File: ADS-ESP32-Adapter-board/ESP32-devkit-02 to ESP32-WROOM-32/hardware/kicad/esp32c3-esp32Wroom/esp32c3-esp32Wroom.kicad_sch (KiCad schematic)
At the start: 4 parts, among them J1 Conn_01x15_esp32_devkit_V1_el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, J2 Conn_01x15_esp32_devkit_V1_el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, J3 Conn_01x15_esp32_c3_devkit_02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, J4 Conn_01x15_esp32_c3_devkit_02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

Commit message: modified
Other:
- company: (none) -> BIOMEC UMA dpto Hardware
- title: (none) -> ESP32-C3-DevkitC-02
- moved on the sheet: J1, J2, J3, J4

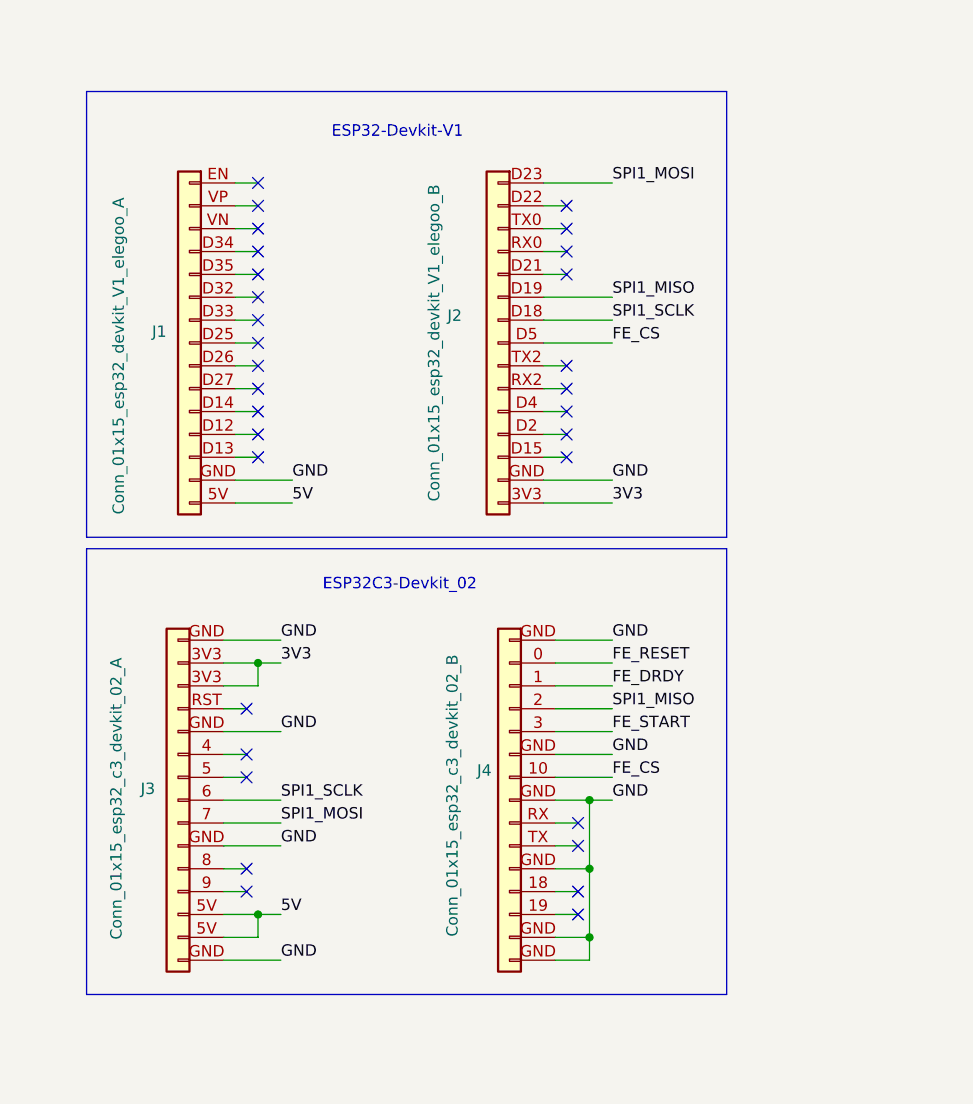
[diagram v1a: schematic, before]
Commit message: Esquema terminado, PCB terminada pero falta agregar algún símbolo que indique la posición, asegurar que las ancho pistas es adecuado y que no haya acoplamiento entre pistas.
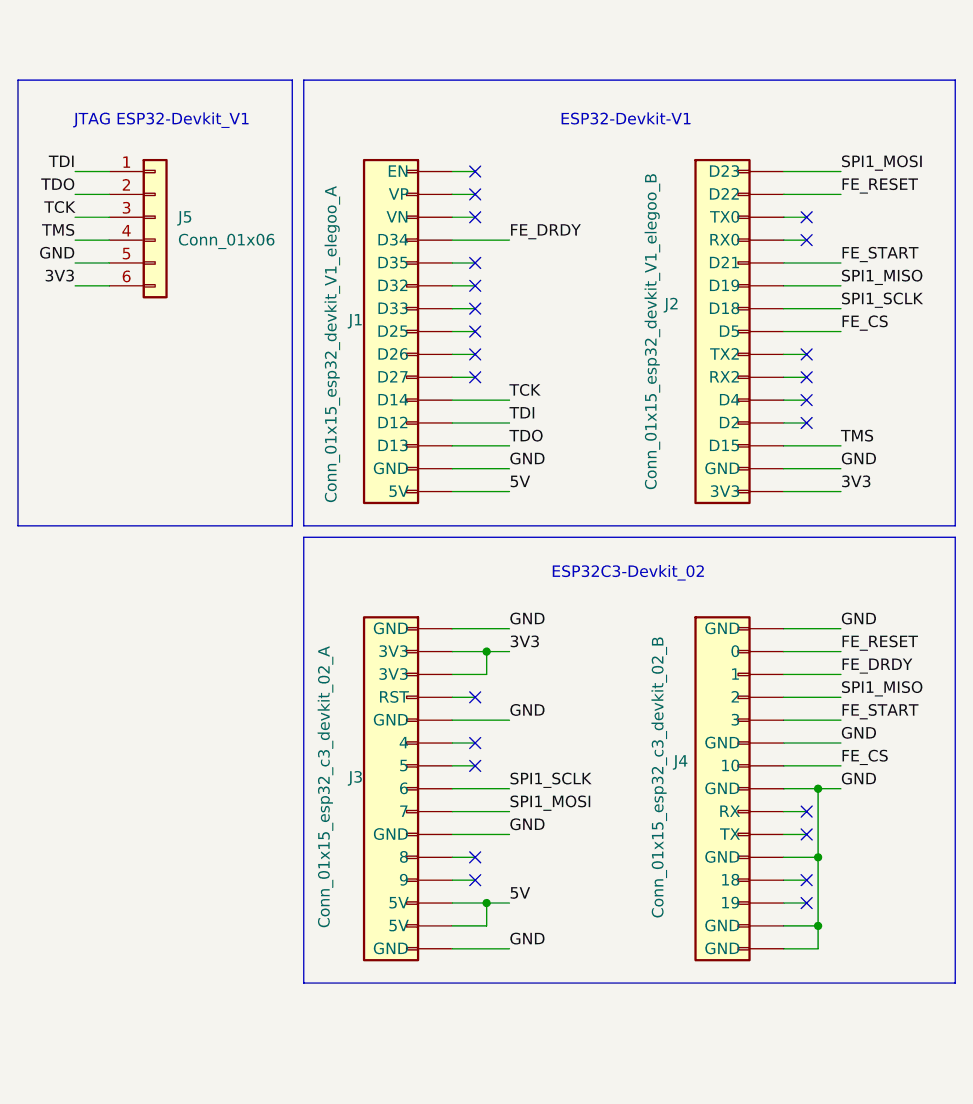
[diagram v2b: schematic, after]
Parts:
- added J5: Conn_01x06, Connector_PinSocket_2.54mm:PinSocket_1x06_P2.54mm_Vertical, symbol Connector_Generic:Conn_01x06
- J1, J2: footprint Connector_PinSocket_2.54mm:PinSocket_1x15_P2.54mm_Vertical -> Connector_PinHeader_2.54mm:PinHeader_1x15_P2.54mm_Vertical
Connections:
- net 3V3: now also J2.15 (3V3), J3.2 (3V3), J3.3 (3V3), J5.6 (Pin_6); no longer J2.3V3 (Pin_15), J3.3V3 (Pin_3)
- net 5V: now also J1.15 (5V), J3.13 (5V), J3.14 (5V); no longer J1.5V (Pin_15), J3.5V (Pin_14)
- net FE_CS: now also J2.8 (D5), J4.7 (10); no longer J2.D5 (Pin_8), J4.10 (Pin_7)
- net FE_DRDY: now also J1.4 (D34), J4.3 (1); no longer J4.1 (Pin_3)
- net FE_RESET: now also J2.2 (D22), J4.2 (0); no longer J4.0 (Pin_2)
- net FE_START: now also J2.5 (D21), J4.5 (3); no longer J4.3 (Pin_5)
- net GND: now also J1.14 (GND), J2.14 (GND), J3.1 (GND), J3.10 (GND), J3.15 (GND), J3.5 (GND), J4.1 (GND), J4.11 (GND), J4.14 (GND), J4.15 (GND), J4.6 (GND), J4.8 (GND), J5.5 (Pin_5); no longer J1.GND (Pin_14), J2.GND (Pin_14), J3.GND (Pin_15), J4.GND (Pin_15)
- net SPI1_MISO: now also J2.6 (D19), J4.4 (2); no longer J2.D19 (Pin_6), J4.2 (Pin_4)
- net SPI1_MOSI: now also J2.1 (D23), J3.9 (7); no longer J2.D23 (Pin_1), J3.7 (Pin_9)
- net SPI1_SCLK: now also J2.7 (D18), J3.8 (6); no longer J2.D18 (Pin_7), J3.6 (Pin_8)
- new net TCK: J1.11 (D14), J5.3 (Pin_3)
- new net TDI: J1.12 (D12), J5.1 (Pin_1)
- new net TDO: J1.13 (D13), J5.2 (Pin_2)
- new net TMS: J2.13 (D15), J5.4 (Pin_4)
- no-connect marks 31 -> 24
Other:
- note added: "JTAG ESP32-Devkit_V1"
- moved on the sheet: J1, J2, J3, J4

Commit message: Refactor code structure for improved readability and maintainability
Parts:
- J1, J2: footprint Connector_PinHeader_2.54mm:PinHeader_1x15_P2.54mm_Vertical -> Connector_PinSocket_2.54mm:PinSocket_1x15_P2.54mm_Vertical
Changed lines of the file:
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@@
 			)
 		)
-		(property "Footprint" "Connector_PinHeader_2.54mm:PinHeader_1x15_P2.54mm_Vertical"
+		(property "Footprint" "Connector_PinSocket_2.54mm:PinSocket_1x15_P2.54mm_Vertical"
 			(at 107.95 52.07 0)
 			(hide yes)
@@
 			)
 		)
-		(property "Footprint" "Connector_PinHeader_2.54mm:PinHeader_1x15_P2.54mm_Vertical"
+		(property "Footprint" "Connector_PinSocket_2.54mm:PinSocket_1x15_P2.54mm_Vertical"
 			(at 73.66 52.07 0)
 			(hide yes)

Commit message: Add additional text annotations to schematic and update visible layers in PCB layout
- Added JTAG, GND, GPIO, Source, and SPI text annotations to the schematic for better clarity and reference.
- Updated the visible layers in the PCB layout file to include grid visibility.
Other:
- note added: "GND"
- note added: "GPIO"
- note added: "JTAG"
- note added: "SPI"
- note added: "Source"
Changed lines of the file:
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@@
+		)
+	)
+	(text "JTAG"
+		(exclude_from_sim no)
+		(at 54.61 18.796 0)
+		(effects
+			(font
+				(size 1.27 1.27)
+				(thickness 0.254)
+				(bold yes)
+				(color 204 102 0 1)
+			)
+		)
+	)
+	(text "GND"
+		(exclude_from_sim no)
+		(at 60.198 18.796 0)
+		(effects
+			(font
+				(size 1.27 1.27)
+				(thickness 0.254)
+				(bold yes)
+				(color 0 0 0 1)
+			)
+		)
+	)
+	(text "GPIO"
+		(exclude_from_sim no)
+		(at 48.006 18.796 0)
+		(effects
+			(font
+				(size 1.27 1.27)
+				(thickness 0.254)
+				(bold yes)
+				(color 0 0 194 1)
+			)
+		)
+	)
+	(text "Source"
+		(exclude_from_sim no)
+		(at 40.132 18.796 0)
+		(effects
+			(font
+				(size 1.27 1.27)
+				(thickness 0.254)
+				(bold yes)
+				(color 194 0 0 1)
+			)
 		)
 	)
@@
 			)
 		)
+	)
+	(text "SPI"
+		(exclude_from_sim no)
+		(at 32.766 19.05 0)
+		(effects
+			(font
+				(size 1.27 1.27)
+				(thickness 0.254)
+				(bold yes)
+				(color 0 132 0 1)
+			)
+		)
